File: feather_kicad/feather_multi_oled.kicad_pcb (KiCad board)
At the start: 2 copper layers, 23 x 120 mm, 72 parts, among them J1 Barrel_Jack_Switch, U1 feather, U10 SSD1309_transparent_oled, U11 SSD1309_transparent_oled, U12 SSD1309_transparent_oled, U13 MPU-6050, U2 SSD1309_transparent_oled, U3 SSD1309_transparent_oled, U4 SSD1309_transparent_oled, U5 SSD1309_transparent_oled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

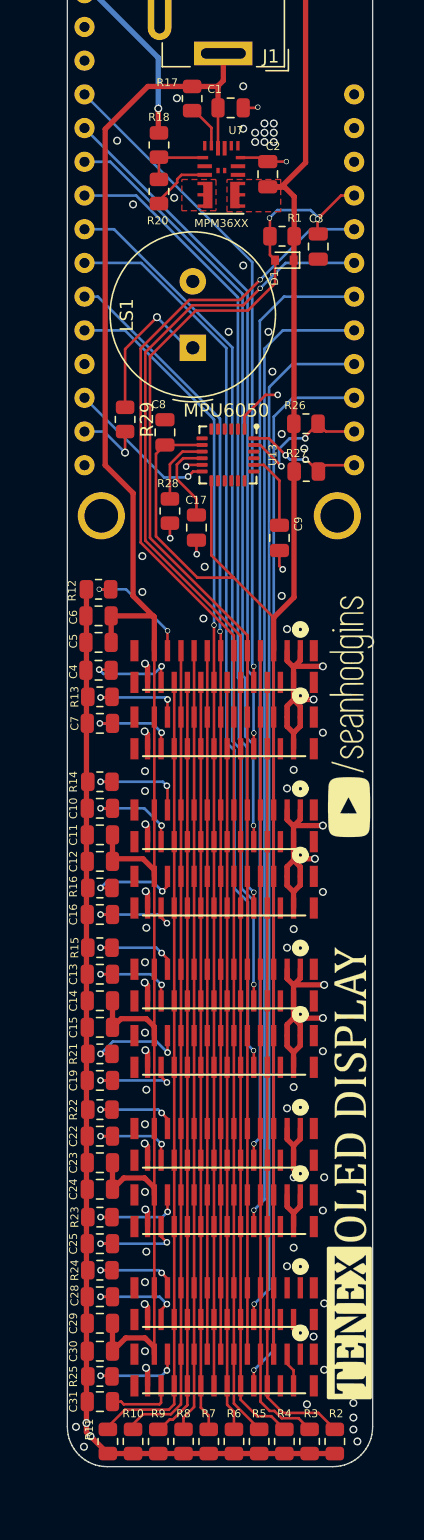
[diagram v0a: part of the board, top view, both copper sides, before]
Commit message: updated BOM for new 24 Pin FCP Connector P/N
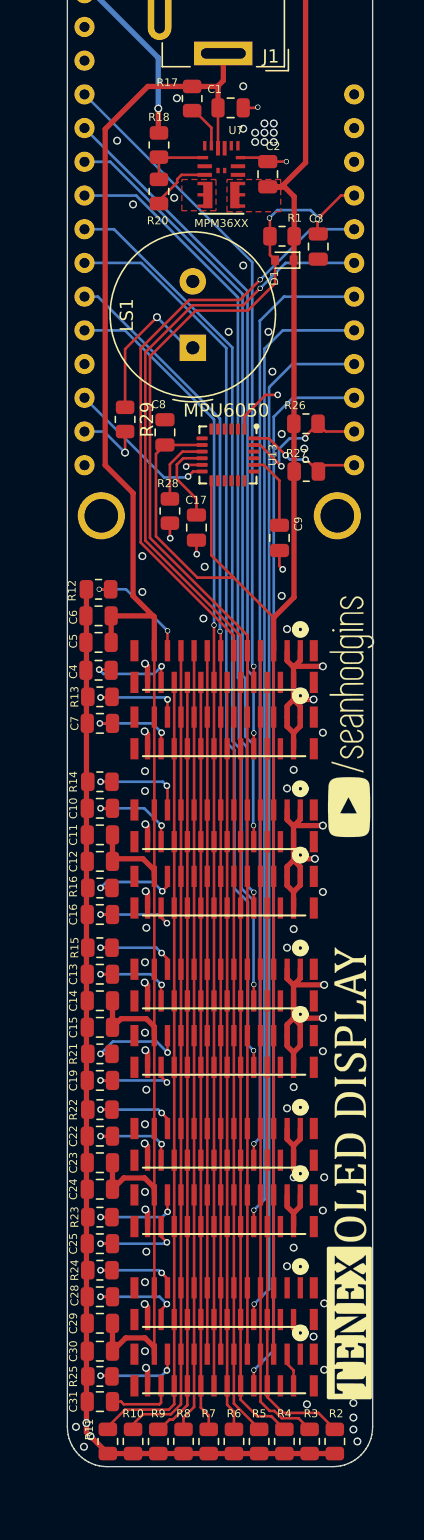
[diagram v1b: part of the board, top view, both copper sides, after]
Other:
- net class Default removed
